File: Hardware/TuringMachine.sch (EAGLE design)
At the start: 82 parts, among them IC1 TL072P, IC2 4015, IC3 4015, IC5 4016, IC6 TL072P, IC7 TL072P, T1 2N3904, T2 2N3904, T3 2N3904

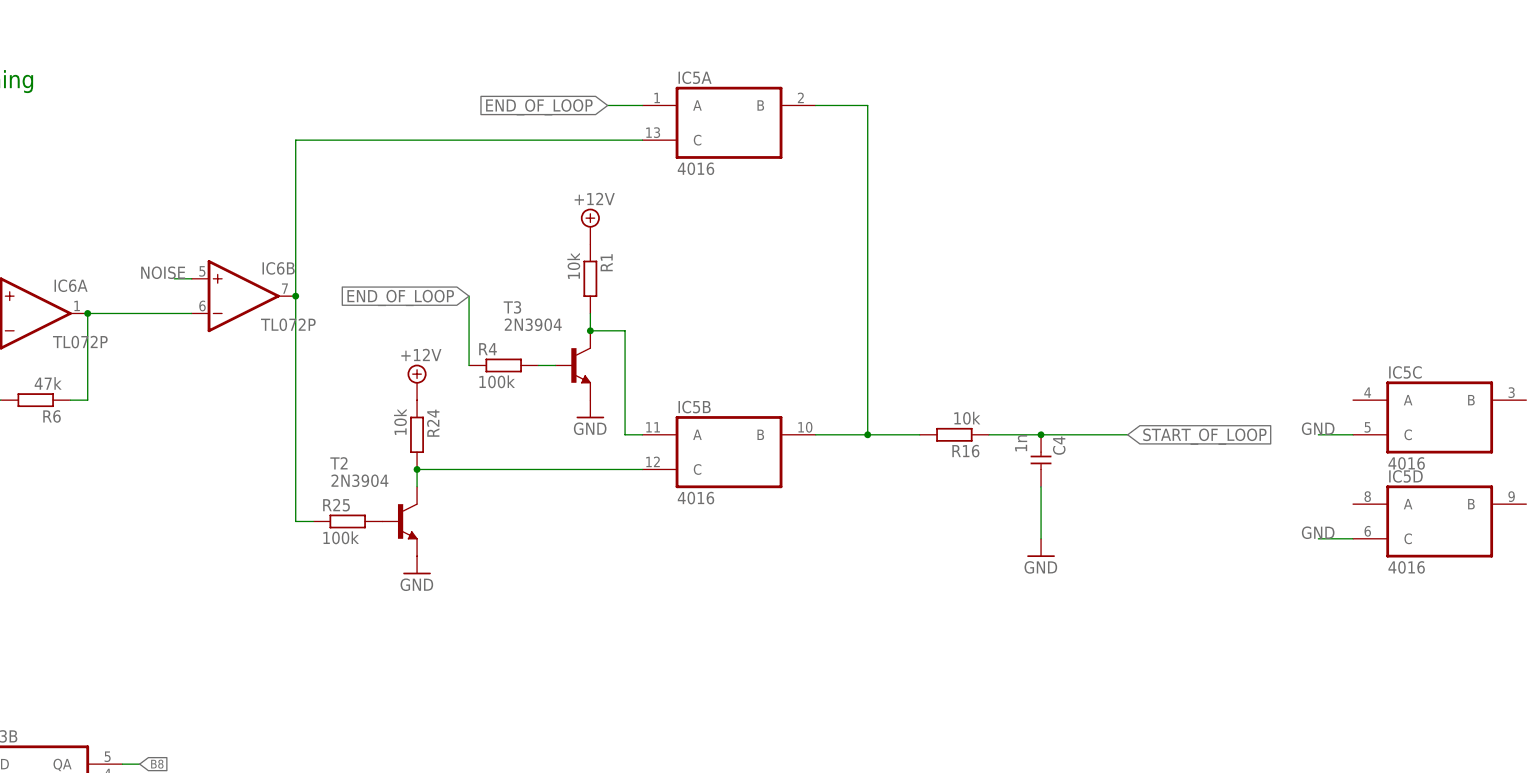
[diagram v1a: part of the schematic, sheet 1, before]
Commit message: Remove transistors, replace with 4016 gates
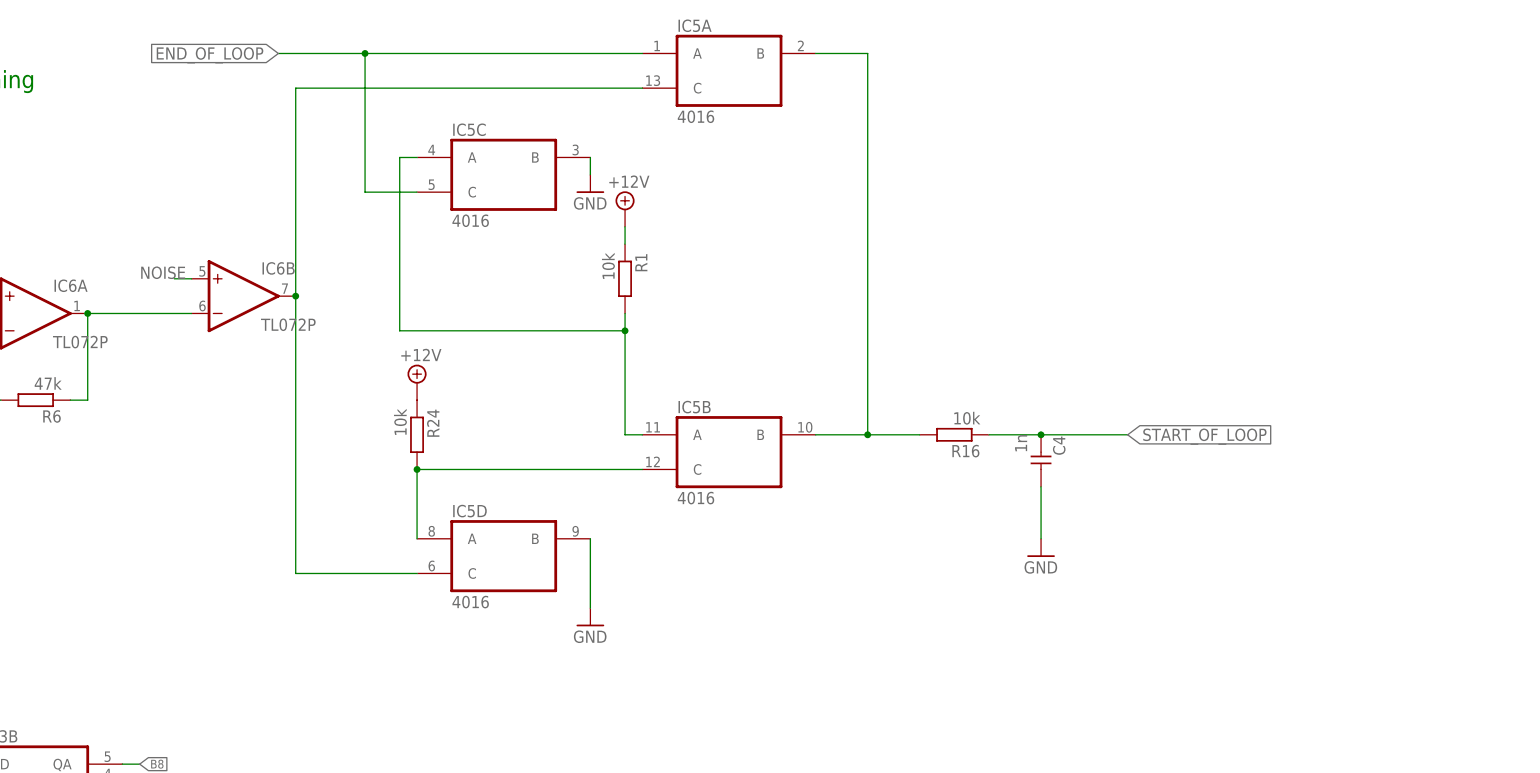
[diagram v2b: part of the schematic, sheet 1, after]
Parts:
- removed R25, R4: 100k, TomW:R-EU_0207/7
- removed T2, T3: 2N3904, transistor:2N3904
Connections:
- removed net N$1: R4.2, T3.B
- removed net N$44: R25.2, T2.B
- net END_OF_LOOP: now also IC5C.C; no longer R4.1
- net GND: now also IC5C.B, IC5D.B; no longer IC5C.C, IC5D.C, T2.E, T3.E
- net N$24: now also IC5D.C; no longer R25.1
- net N$4: now also IC5C.A; no longer T3.C
- net N$45: now also IC5D.A; no longer T2.C
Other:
- moved on the sheet: IC5A, IC5C, IC5D, R1
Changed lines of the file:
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@@
 <part name="EXPANSION" library="TomW" deviceset="MA10-1" device=""/>
 <part name="IC5" library="40xx" deviceset="4016" device="N" value="4016"/>
-<part name="T2" library="transistor" deviceset="2N3904" device=""/>
 <part name="GND20" library="SparkFun-Aesthetics" deviceset="GND" device=""/>
 <part name="R24" library="TomW" deviceset="R-EU_" device="0207/7" value="10k"/>
-<part name="R25" library="TomW" deviceset="R-EU_" device="0207/7" value="100k"/>
 <part name="P+6" library="supply2" deviceset="+12V" device=""/>
 <part name="R22" library="TomW" deviceset="R-EU_" device="0207/7" value="100k"/>
@@
 <part name="P+7" library="supply2" deviceset="+12V" device=""/>
 <part name="SUPPLY11" library="supply2" deviceset="-12V" device=""/>
-<part name="T3" library="transistor" deviceset="2N3904" device=""/>
 <part name="GND3" library="SparkFun-Aesthetics" deviceset="GND" device=""/>
 <part name="R1" library="TomW" deviceset="R-EU_" device="0207/7" value="10k"/>
-<part name="R4" library="TomW" deviceset="R-EU_" device="0207/7" value="100k"/>
 <part name="P+1" library="supply2" deviceset="+12V" device=""/>
 <part name="CV_IN" library="MusicThingModular" deviceset="THONKICONN" device=""/>
@@
 <instance part="GND15" gate="1" x="76.2" y="81.28"/>
 <instance part="IC6" gate="B" x="121.92" y="134.62"/>
-<instance part="IC5" gate="A" x="193.04" y="160.02"/>
+<instance part="IC5" gate="A" x="193.04" y="167.64"/>
 <instance part="IC5" gate="B" x="193.04" y="111.76"/>
-<instance part="T2" gate="G1" x="144.78" y="101.6"/>
-<instance part="GND20" gate="1" x="147.32" y="93.98"/>
+<instance part="GND20" gate="1" x="172.72" y="86.36"/>
 <instance part="R24" gate="G$1" x="147.32" y="114.3" rot="R270"/>
-<instance part="R25" gate="G$1" x="137.16" y="101.6"/>
 <instance part="P+6" gate="+12V" x="147.32" y="121.92"/>
 <instance part="R22" gate="G$1" x="63.5" y="144.78" rot="R180"/>
@@
 <instance part="P+7" gate="+12V" x="58.42" y="154.94"/>
 <instance part="SUPPLY11" gate="G$1" x="58.42" y="134.62"/>
-<instance part="T3" gate="G1" x="170.18" y="124.46"/>
-<instance part="GND3" gate="1" x="172.72" y="116.84"/>
-<instance part="R1" gate="G$1" x="172.72" y="137.16" rot="R270"/>
-<instance part="R4" gate="G$1" x="160.02" y="124.46"/>
-<instance part="P+1" gate="+12V" x="172.72" y="144.78"/>
+<instance part="GND3" gate="1" x="172.72" y="149.86"/>
+<instance part="R1" gate="G$1" x="177.8" y="137.16" rot="R270"/>
+<instance part="P+1" gate="+12V" x="177.8" y="147.32"/>
 <instance part="CV_IN" gate="G$1" x="45.72" y="121.92" rot="R180"/>
 <instance part="R5" gate="G$1" x="63.5" y="119.38"/>
 <instance part="GND16" gate="1" x="81.28" y="132.08"/>
 <instance part="R6" gate="G$1" x="91.44" y="119.38" rot="R180"/>
-<instance part="IC5" gate="C" x="297.18" y="116.84"/>
-<instance part="IC5" gate="D" x="297.18" y="101.6"/>
+<instance part="IC5" gate="C" x="160.02" y="152.4"/>
+<instance part="IC5" gate="D" x="160.02" y="96.52"/>
 <instance part="IC6" gate="A" x="91.44" y="132.08"/>
 <instance part="U$1" gate="G$1" x="203.2" y="17.78" rot="R90"/>
@@
 <pinref part="R1" gate="G$1" pin="1"/>
 <pinref part="P+1" gate="+12V" pin="+12V"/>
+<wire x1="177.8" y1="142.24" x2="177.8" y2="144.78" width="0.1524" layer="91"/>
 </segment>
 </net>
@@
 </segment>
 <segment>
-<pinref part="T2" gate="G1" pin="E"/>
 <pinref part="GND20" gate="1" pin="GND"/>
-</segment>
-<segment>
-<pinref part="T3" gate="G1" pin="E"/>
-<pinref part="GND3" gate="1" pin="GND"/>
+<wire x1="172.72" y1="88.9" x2="172.72" y2="99.06" width="0.1524" layer="91"/>
+<pinref part="IC5" gate="D" pin="B"/>
 </segment>
 <segment>
@@
 </segment>
 <segment>
-<pinref part="IC5" gate="C" pin="C"/>
-<wire x1="279.4" y1="114.3" x2="284.48" y2="114.3" width="0.1524" layer="91"/>
-<label x="276.86" y="114.3" size="1.778" layer="95"/>
-</segment>
-<segment>
-<pinref part="IC5" gate="D" pin="C"/>
-<wire x1="279.4" y1="99.06" x2="284.48" y2="99.06" width="0.1524" layer="91"/>
-<label x="276.86" y="99.06" size="1.778" layer="95"/>
-</segment>
-<segment>
 <pinref part="VR2" gate="G$1" pin="P$1"/>
 <pinref part="GND31" gate="1" pin="GND"/>
 <wire x1="33.02" y1="139.7" x2="33.02" y2="144.78" width="0.1524" layer="91"/>
+</segment>
+<segment>
+<pinref part="IC5" gate="C" pin="B"/>
+<pinref part="GND3" gate="1" pin="GND"/>
+<wire x1="172.72" y1="152.4" x2="172.72" y2="154.94" width="0.1524" layer="91"/>
 </segment>
 </net>
@@
 <wire x1="205.74" y1="114.3" x2="213.36" y2="114.3" width="0.1524" layer="91"/>
 <pinref part="IC5" gate="A" pin="B"/>
-<wire x1="205.74" y1="162.56" x2="213.36" y2="162.56" width="0.1524" layer="91"/>
-<wire x1="213.36" y1="162.56" x2="213.36" y2="114.3" width="0.1524" layer="91"/>
+<wire x1="205.74" y1="170.18" x2="213.36" y2="170.18" width="0.1524" layer="91"/>
+<wire x1="213.36" y1="170.18" x2="213.36" y2="114.3" width="0.1524" layer="91"/>
 <pinref part="R16" gate="G$1" pin="2"/>
 <wire x1="220.98" y1="114.3" x2="213.36" y2="114.3" width="0.1524" layer="91"/>
@@
 </segment>
 </net>
-<net name="N$44" class="0">
-<segment>
-<pinref part="T2" gate="G1" pin="B"/>
-<pinref part="R25" gate="G$1" pin="2"/>
-</segment>
-</net>
 <net name="N$45" class="0">
 <segment>
-<pinref part="T2" gate="G1" pin="C"/>
 <pinref part="R24" gate="G$1" pin="2"/>
-<wire x1="147.32" y1="109.22" x2="147.32" y2="106.68" width="0.1524" layer="91"/>
+<wire x1="147.32" y1="109.22" x2="147.32" y2="99.06" width="0.1524" layer="91"/>
 <wire x1="147.32" y1="109.22" x2="180.34" y2="109.22" width="0.1524" layer="91"/>
 <junction x="147.32" y="109.22"/>
 <pinref part="IC5" gate="B" pin="C"/>
+<pinref part="IC5" gate="D" pin="A"/>
 </segment>
 </net>
@@
 <segment>
 <pinref part="IC6" gate="B" pin="OUT"/>
-<pinref part="R25" gate="G$1" pin="1"/>
-<wire x1="132.08" y1="101.6" x2="129.54" y2="101.6" width="0.1524" layer="91"/>
-<wire x1="129.54" y1="134.62" x2="129.54" y2="101.6" width="0.1524" layer="91"/>
-<wire x1="129.54" y1="134.62" x2="129.54" y2="157.48" width="0.1524" layer="91"/>
+<wire x1="147.32" y1="93.98" x2="129.54" y2="93.98" width="0.1524" layer="91"/>
+<wire x1="129.54" y1="134.62" x2="129.54" y2="93.98" width="0.1524" layer="91"/>
+<wire x1="129.54" y1="134.62" x2="129.54" y2="165.1" width="0.1524" layer="91"/>
 <junction x="129.54" y="134.62"/>
 <pinref part="IC5" gate="A" pin="C"/>
-<wire x1="129.54" y1="157.48" x2="180.34" y2="157.48" width="0.1524" layer="91"/>
+<wire x1="129.54" y1="165.1" x2="180.34" y2="165.1" width="0.1524" layer="91"/>
+<pinref part="IC5" gate="D" pin="C"/>
 </segment>
 </net>
@@
 <segment>
 <pinref part="IC5" gate="A" pin="A"/>
-<wire x1="175.26" y1="162.56" x2="180.34" y2="162.56" width="0.1524" layer="91"/>
-<label x="175.26" y="162.56" size="1.778" layer="95" rot="R180" xref="yes"/>
-</segment>
-<segment>
-<pinref part="R4" gate="G$1" pin="1"/>
-<wire x1="154.94" y1="134.62" x2="154.94" y2="124.46" width="0.1524" layer="91"/>
-<label x="154.94" y="134.62" size="1.778" layer="95" rot="R180" xref="yes"/>
-</segment>
-</net>
-<net name="N$1" class="0">
-<segment>
-<pinref part="T3" gate="G1" pin="B"/>
-<pinref part="R4" gate="G$1" pin="2"/>
-<wire x1="165.1" y1="124.46" x2="167.64" y2="124.46" width="0.1524" layer="91"/>
+<wire x1="127" y1="170.18" x2="139.7" y2="170.18" width="0.1524" layer="91"/>
+<label x="127" y="170.18" size="1.778" layer="95" rot="R180" xref="yes"/>
+<pinref part="IC5" gate="C" pin="C"/>
+<wire x1="139.7" y1="170.18" x2="180.34" y2="170.18" width="0.1524" layer="91"/>
+<wire x1="147.32" y1="149.86" x2="139.7" y2="149.86" width="0.1524" layer="91"/>
+<wire x1="139.7" y1="149.86" x2="139.7" y2="170.18" width="0.1524" layer="91"/>
+<junction x="139.7" y="170.18"/>
 </segment>
 </net>
@@
 <net name="N$4" class="0">
 <segment>
-<pinref part="T3" gate="G1" pin="C"/>
 <pinref part="R1" gate="G$1" pin="2"/>
-<wire x1="172.72" y1="132.08" x2="172.72" y2="129.54" width="0.1524" layer="91"/>
-<wire x1="172.72" y1="129.54" x2="177.8" y2="129.54" width="0.1524" layer="91"/>
+<wire x1="177.8" y1="132.08" x2="177.8" y2="129.54" width="0.1524" layer="91"/>
+<pinref part="IC5" gate="B" pin="A"/>
 <wire x1="177.8" y1="129.54" x2="177.8" y2="114.3" width="0.1524" layer="91"/>
-<junction x="172.72" y="129.54"/>
-<pinref part="IC5" gate="B" pin="A"/>
 <wire x1="177.8" y1="114.3" x2="180.34" y2="114.3" width="0.1524" layer="91"/>
-</segment>
-</net>
+<pinref part="IC5" gate="C" pin="A"/>
+<wire x1="147.32" y1="154.94" x2="144.78" y2="154.94" width="0.1524" layer="91"/>
+<wire x1="144.78" y1="154.94" x2="144.78" y2="129.54" width="0.1524" layer="91"/>
+<wire x1="144.78" y1="129.54" x2="177.8" y2="129.54" width="0.1524" layer="91"/>
+<junction x="177.8" y="129.54"/>
+</segment>
+</net>
